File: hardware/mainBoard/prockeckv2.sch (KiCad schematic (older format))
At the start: 20 parts

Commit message: Added the power part of the schematic
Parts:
- removed C?: 0.1uF, Capacitor_SMD:C_0603_1608Metric_Pad1.05x0.95mm_HandSolder, symbol Device:C_Small
- removed C?: 10uF, Capacitor_SMD:C_0805_2012Metric_Pad1.15x1.40mm_HandSolder, symbol Device:C_Small
- removed C?: 0.1u, Capacitor_SMD:C_0603_1608Metric_Pad1.05x0.95mm_HandSolder, symbol Device:C_Small
- removed D?: SS3150, Diode_SMD:D_SMC_Handsoldering, symbol Device:D
- removed IC?: DW01A, Package_TO_SOT_SMD:SOT-23-6, symbol forcenOne-rescue:DW01A-chinaland
- removed J?: BATT, Connector_PinHeader_2.54mm:PinHeader_1x02_P2.54mm_Vertical, symbol Connector_Generic:Conn_01x02
- removed M?: FS8205A, Package_SO:TSSOP-8_4.4x3mm_P0.65mm, symbol forcenOne-rescue:FS8205A-chinaland
- removed Q?: CJ2301, Package_TO_SOT_SMD:SOT-23_Handsoldering, symbol Device:Q_PMOS_GSD
- removed R?: 1k, Resistor_SMD:R_0603_1608Metric_Pad1.05x0.95mm_HandSolder, symbol Device:R_Small
- removed R?: 100, Resistor_SMD:R_0603_1608Metric_Pad1.05x0.95mm_HandSolder, symbol Device:R_Small
- removed R? (x2): 10k, Resistor_SMD:R_0603_1608Metric_Pad1.05x0.95mm_HandSolder, symbol Device:R_Small
- removed R?: 1k2, Resistor_SMD:R_0603_1608Metric_Pad1.05x0.95mm_HandSolder, symbol Device:R_Small
- removed R?: 100k, Resistor_SMD:R_0603_1608Metric_Pad1.05x0.95mm_HandSolder, symbol Device:R_Small
- removed U?: TP4056, Package_SO:HSOP-8-1EP_3.9x4.9mm_P1.27mm_EP2.41x3.1mm_ThermalVias, symbol forcenOne-rescue:TP4056-chinaland
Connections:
- net labels removed: CHRG, STDBY, VPow, Vbatt
- wire segments 100 -> 15
- no-connect marks 4 -> 2
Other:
- note removed: "Cargador de batería con circuito protector"
- note removed: "Conmutador de energía"
- note removed: "Cuando Vusb>Vbat no conduce\nVusb<Vbat-1"

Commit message: Added external connections, analog conditioning and several items
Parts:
- removed D?: LED, LED_SMD:LED_0603_1608Metric_Pad1.05x0.95mm_HandSolder, symbol Device:LED
- removed R?: 10k, Resistor_SMD:R_0603_1608Metric_Pad1.05x0.95mm_HandSolder, symbol Device:R
- removed R?: 220, Resistor_SMD:R_0603_1608Metric_Pad1.05x0.95mm_HandSolder, symbol Device:R
- removed SW?: SW_Push, Button_Switch_THT:SW_PUSH_6mm, symbol Switch:SW_Push
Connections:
- net labels added: USB_D+, USB_D-
- net labels removed: +5V, LED, RST, UD+, UD-
- wire segments 15 -> 7
- no-connect marks 2 -> 1
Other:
- note removed: "Digital"
- note removed: "Others"
- note removed: "Power Supply"
- moved on the sheet: J?

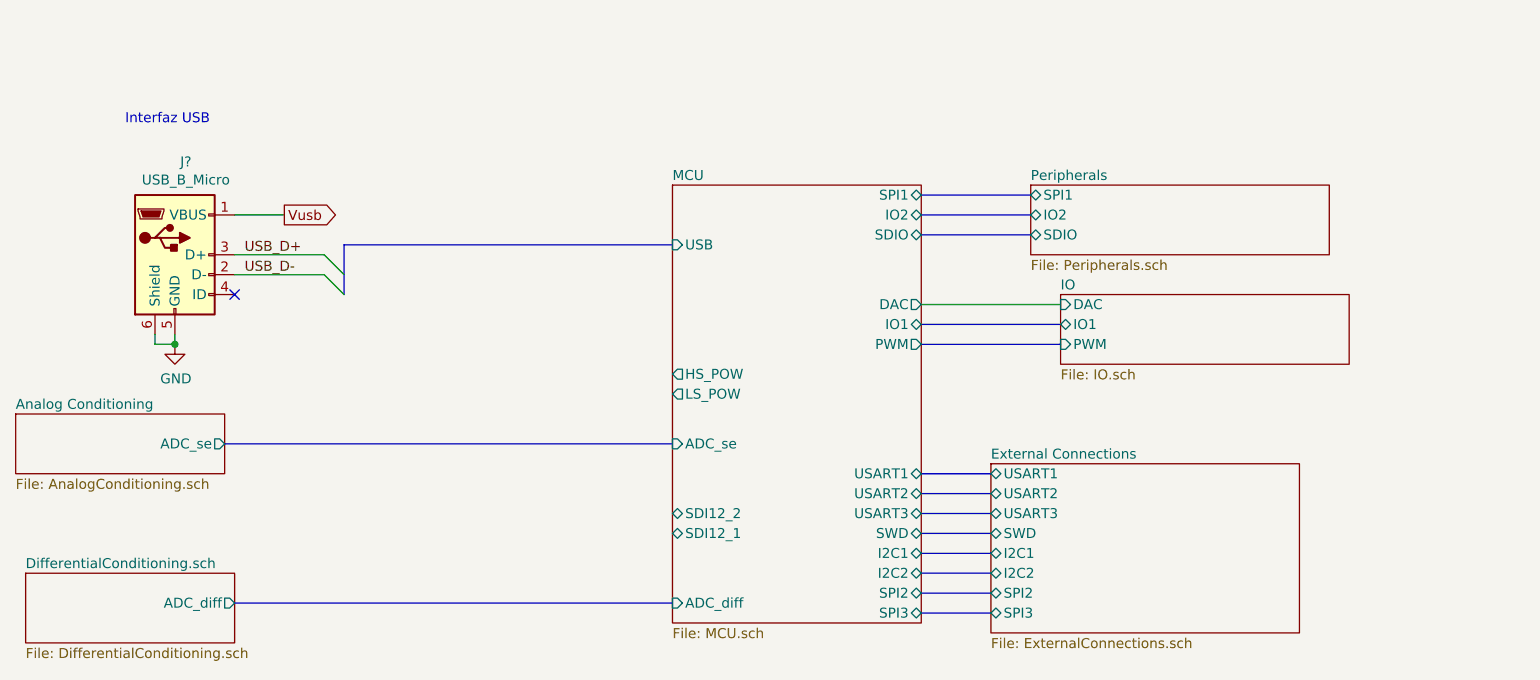
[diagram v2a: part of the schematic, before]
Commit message: Ended schematic, created some pcb footprints
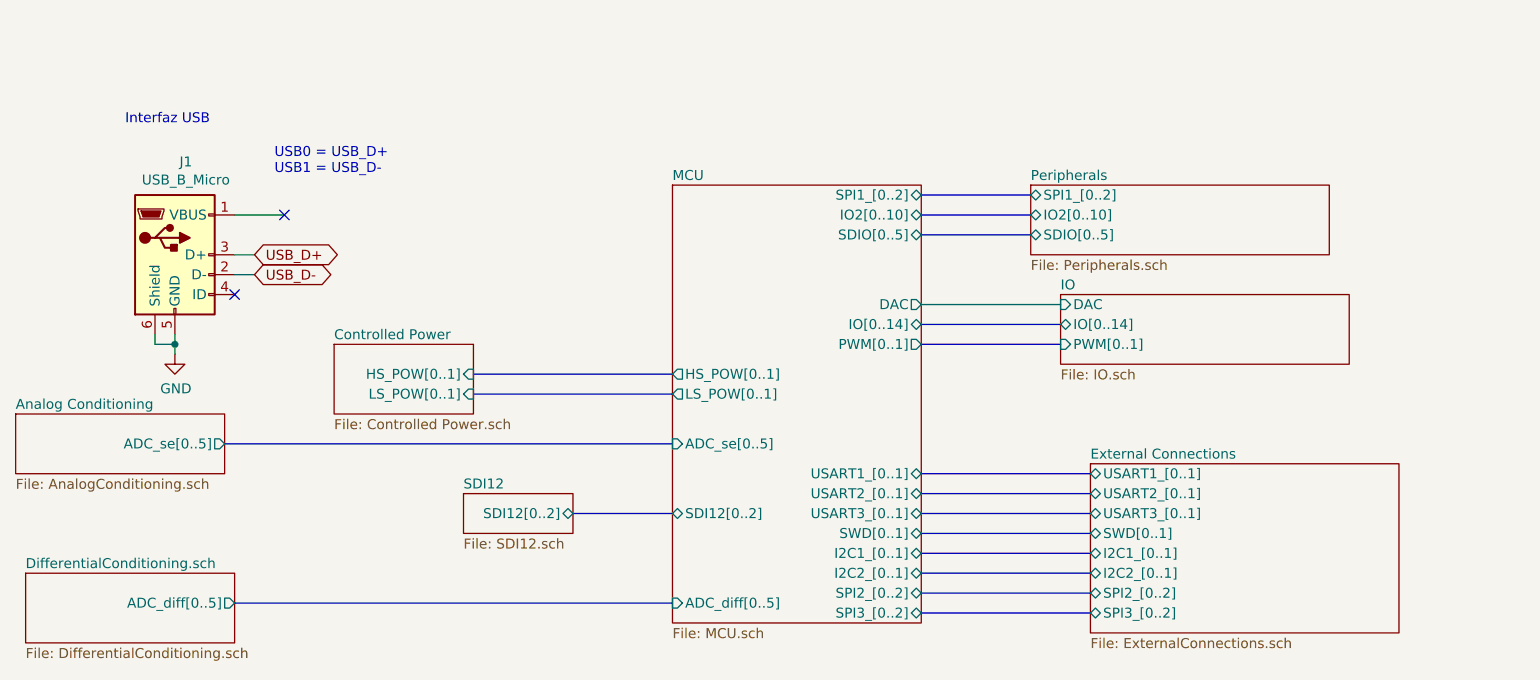
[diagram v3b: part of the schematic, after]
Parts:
- gave numbers to parts that had none: 1
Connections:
- net Vusb: no longer names the net of J1.1 (VBUS)
- no-connect marks 1 -> 2
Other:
- note added: "USB0 = USB_D+\nUSB1 = USB_D-"
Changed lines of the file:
@@
 $Descr A4 11693 8268
 encoding utf-8
-Sheet 1 8
+Sheet 1 10
 Title "Procheck V2"
 Date ""
@@
 F0 "IO" 50
 F1 "IO.sch" 50
-F2 "IO1" B L 7300 3550 50
+F2 "IO[0..14]" B L 7300 3550 50
 F3 "DAC" I L 7300 3450 50
-F4 "PWM" I L 7300 3650 50
+F4 "PWM[0..1]" I L 7300 3650 50
 $EndSheet
 $Sheet
@@
 F0 "Peripherals" 50
 F1 "Peripherals.sch" 50
-F2 "SPI1" B L 7150 2900 50
-F3 "IO2" B L 7150 3000 50
-F4 "SDIO" B L 7150 3100 50
+F2 "SPI1_[0..2]" B L 7150 2900 50
+F3 "IO2[0..10]" B L 7150 3000 50
+F4 "SDIO[0..5]" B L 7150 3100 50
 $EndSheet
 $Comp
-L Connector:USB_B_Micro J?
+L Connector:USB_B_Micro J1
 U 1 1 5C742C3D
 P 2850 3200
-F 0 "J?" H 2905 3667 50  0000 C CNN
+F 0 "J1" H 2905 3667 50  0000 C CNN
 F 1 "USB_B_Micro" H 2905 3576 50  0000 C CNN
 F 2 "Connector_USB:USB_Micro-B_Molex-105017-0001" H 3000 3150 50  0001 C CNN
@@
 Wire Wire Line
 	3150 3000 3400 3000
-Text GLabel 3400 3000 2    50   Output ~ 0
-Vusb
 $Comp
-L power:GND #PWR?
+L power:GND #PWR01
 U 1 1 5CA32110
-P 2850 3650
-F 0 "#PWR?" H 2850 3400 50  0001 C CNN
-F 1 "GND" H 2855 3477 50  0000 C CNN
-F 2 "" H 2850 3650 50  0001 C CNN
-F 3 "" H 2850 3650 50  0001 C CNN
-	1    2850 3650
+P 2850 3700
+F 0 "#PWR01" H 2850 3450 50  0001 C CNN
+F 1 "GND" H 2855 3527 50  0000 C CNN
+F 2 "" H 2850 3700 50  0001 C CNN
+F 3 "" H 2850 3700 50  0001 C CNN
+	1    2850 3700
 	1    0    0    -1
 $EndComp
@@
 Text Notes 2600 2550 0    50   ~ 0
 Interfaz USB
-Wire Wire Line
-	3150 3300 3600 3300
-Wire Wire Line
-	3150 3200 3600 3200
 Wire Wire Line
 	2850 3600 2850 3650
@@
 F0 "MCU" 50
 F1 "MCU.sch" 50
-F2 "USB" I L 5350 3150 50
-F3 "SPI1" B R 6600 2900 50
-F4 "IO2" B R 6600 3000 50
-F5 "SDIO" B R 6600 3100 50
-F6 "ADC_se" I L 5350 4150 50
-F7 "ADC_diff" I L 5350 4950 50
-F8 "IO1" B R 6600 3550 50
-F9 "DAC" O R 6600 3450 50
-F10 "USART1" B R 6600 4300 50
-F11 "SWD" B R 6600 4600 50
-F12 "SPI3" B R 6600 5000 50
-F13 "I2C1" B R 6600 4700 50
-F14 "SPI2" B R 6600 4900 50
-F15 "I2C2" B R 6600 4800 50
-F16 "USART2" B R 6600 4400 50
-F17 "USART3" B R 6600 4500 50
-F18 "LS_POW" O L 5350 3900 50
-F19 "SDI12_1" B L 5350 4600 50
-F20 "SDI12_2" B L 5350 4500 50
-F21 "HS_POW" O L 5350 3800 50
-F22 "PWM" O R 6600 3650 50
+F2 "SPI1_[0..2]" B R 6600 2900 50
+F3 "IO2[0..10]" B R 6600 3000 50
+F4 "SDIO[0..5]" B R 6600 3100 50
+F5 "ADC_se[0..5]" I L 5350 4150 50
+F6 "ADC_diff[0..5]" I L 5350 4950 50
+F7 "IO[0..14]" B R 6600 3550 50
+F8 "DAC" O R 6600 3450 50
+F9 "USART1_[0..1]" B R 6600 4300 50
+F10 "SWD[0..1]" B R 6600 4600 50
+F11 "SPI3_[0..2]" B R 6600 5000 50
+F12 "I2C1_[0..1]" B R 6600 4700 50
+F13 "SPI2_[0..2]" B R 6600 4900 50
+F14 "I2C2_[0..1]" B R 6600 4800 50
+F15 "USART2_[0..1]" B R 6600 4400 50
+F16 "USART3_[0..1]" B R 6600 4500 50
+F17 "LS_POW[0..1]" O L 5350 3900 50
+F18 "SDI12[0..2]" B L 5350 4500 50
+F19 "HS_POW[0..1]" O L 5350 3800 50
+F20 "PWM[0..1]" O R 6600 3650 50
 $EndSheet
-Text Label 3200 3200 0    50   ~ 0
-USB_D+
-Text Label 3200 3300 0    50   ~ 0
-USB_D-
-Entry Wire Line
-	3600 3200 3700 3300
-Entry Wire Line
-	3600 3300 3700 3400
-Wire Bus Line
-	3700 3150 5350 3150
 $Sheet
 S 2050 4000 1050 300
@@
 F0 "Analog Conditioning" 50
 F1 "AnalogConditioning.sch" 50
-F2 "ADC_se" O R 3100 4150 50
+F2 "ADC_se[0..5]" O R 3100 4150 50
 $EndSheet
 Wire Bus Line
@@
 F0 "DifferentialConditioning.sch" 50
 F1 "DifferentialConditioning.sch" 50
-F2 "ADC_diff" O R 3150 4950 50
+F2 "ADC_diff[0..5]" O R 3150 4950 50
 $EndSheet
 Wire Bus Line
 	6600 3550 7300 3550
-$Sheet
-S 6950 4250 1550 850
-U 5E56C3C6
-F0 "External Connections" 50
-F1 "ExternalConnections.sch" 50
-F2 "USART1" B L 6950 4300 50
-F3 "USART2" B L 6950 4400 50
-F4 "USART3" B L 6950 4500 50
-F5 "I2C1" B L 6950 4700 50
-F6 "I2C2" B L 6950 4800 50
-F7 "SPI2" B L 6950 4900 50
-F8 "SPI3" B L 6950 5000 50
-F9 "SWD" B L 6950 4600 50
-$EndSheet
 Wire Wire Line
 	6600 3450 7300 3450
@@
 Wire Bus Line
 	6600 3650 7300 3650
+$Sheet
+S 4300 4400 550  200
+U 5DF01F26
+F0 "SDI12" 50
+F1 "SDI12.sch" 50
+F2 "SDI12[0..2]" B R 4850 4500 50
+$EndSheet
 Wire Bus Line
-	6600 4300 6950 4300
+	4850 4500 5350 4500
+$Sheet
+S 3650 3650 700  350
+U 5E0359E0
+F0 "Controlled Power" 50
+F1 "Controlled Power.sch" 50
+F2 "HS_POW[0..1]" I R 4350 3800 50
+F3 "LS_POW[0..1]" I R 4350 3900 50
+$EndSheet
 Wire Bus Line
-	6600 4400 6950 4400
+	4350 3800 5350 3800
 Wire Bus Line
-	6600 4500 6950 4500
+	4350 3900 5350 3900
 Wire Bus Line
-	6600 4600 6950 4600
+	6600 4600 7450 4600
 Wire Bus Line
-	6600 4700 6950 4700
+	6600 5000 7450 5000
 Wire Bus Line
-	6600 4800 6950 4800
+	6600 4900 7450 4900
 Wire Bus Line
-	6600 4900 6950 4900
+	6600 4800 7450 4800
 Wire Bus Line
-	6600 5000 6950 5000
+	6600 4700 7450 4700
 Wire Bus Line
-	3700 3150 3700 3400
+	6600 4500 7450 4500
+Wire Bus Line
+	6600 4400 7450 4400
+Wire Bus Line
+	6600 4300 7450 4300
+$Sheet
+S 7450 4250 1550 850
+U 5E56C3C6
+F0 "External Connections" 50
+F1 "ExternalConnections.sch" 50
+F2 "USART1_[0..1]" B L 7450 4300 50
+F3 "USART2_[0..1]" B L 7450 4400 50
+F4 "USART3_[0..1]" B L 7450 4500 50
+F5 "I2C1_[0..1]" B L 7450 4700 50
+F6 "I2C2_[0..1]" B L 7450 4800 50
+F7 "SPI2_[0..2]" B L 7450 4900 50
+F8 "SPI3_[0..2]" B L 7450 5000 50
+F9 "SWD[0..1]" B L 7450 4600 50
+$EndSheet
+Text Notes 3350 2800 0    50   ~ 0
+USB0 = USB_D+\nUSB1 = USB_D-
+NoConn ~ 3400 3000
+Wire Wire Line
+	2850 3700 2850 3650
+Text GLabel 3250 3200 2    50   BiDi ~ 0
+USB_D+
+Text GLabel 3250 3300 2    50   BiDi ~ 0
+USB_D-
+Wire Wire Line
+	3250 3300 3150 3300
+Wire Wire Line
+	3150 3200 3250 3200
 $EndSCHEMATC

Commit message: First working software
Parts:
- J1: URL (none) -> https://lcsc.com/product-detail/Micro-USB-Connectors_Korean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
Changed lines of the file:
@@
 EESchema Schematic File Version 4
+LIBS:prockeckv2-cache
 EELAYER 30 0
 EELAYER END
@@
 F 2 "Connector_USB:USB_Micro-B_Molex-105017-0001" H 3000 3150 50  0001 C CNN
 F 3 "~" H 3000 3150 50  0001 C CNN
+F 4 "https://lcsc.com/product-detail/Micro-USB-Connectors_Korean-Hroparts-Elec-U-F-M5DD-Y-L_C91146.html" H 2850 3200 50  0001 C CNN "URL"
 	1    2850 3200
 	1    0    0    -1
